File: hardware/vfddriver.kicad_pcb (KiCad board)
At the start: 2 copper layers, 75 x 40 mm, 36 parts, among them J1 Connection Header, U1 IVL2-5_7, U2 LM4871MX_NOPB, U3 LM2733YMF, U4 HV5812WG

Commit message: add research notes about vfds in general
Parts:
- R14: value 4.7kΩ -> 47kΩ

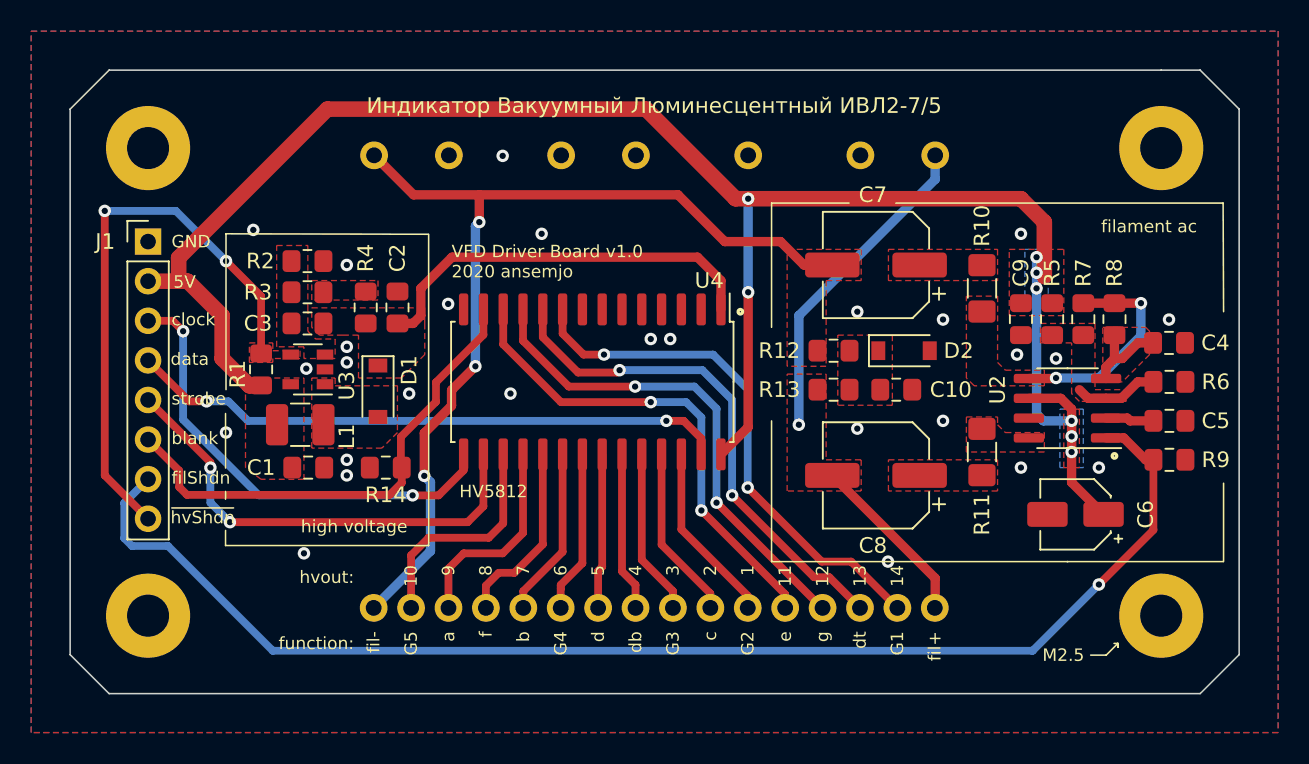
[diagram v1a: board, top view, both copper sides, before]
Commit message: hardware: tidy up, fix photodiode, (re)export (i)boms and schematics
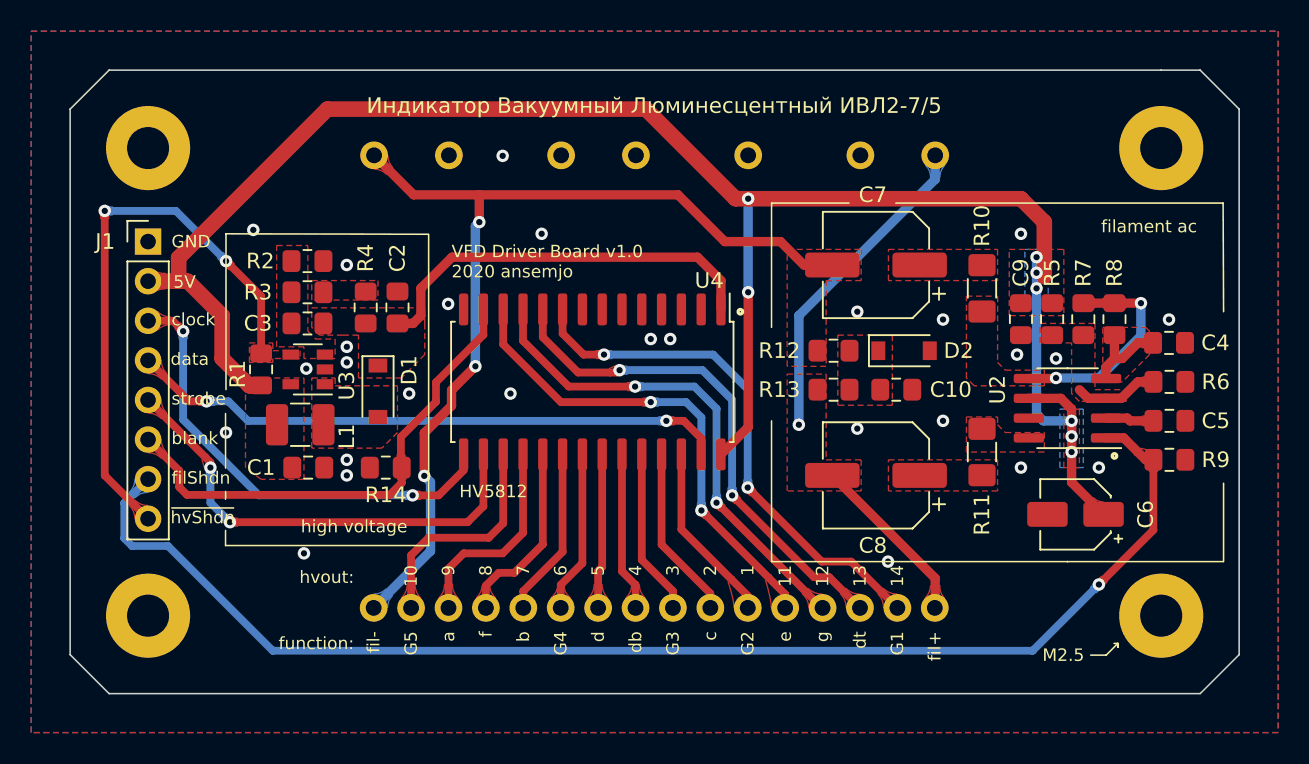
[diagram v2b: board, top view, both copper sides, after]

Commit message: hw: [WIP] add attiny412, remove traces in prep for v2
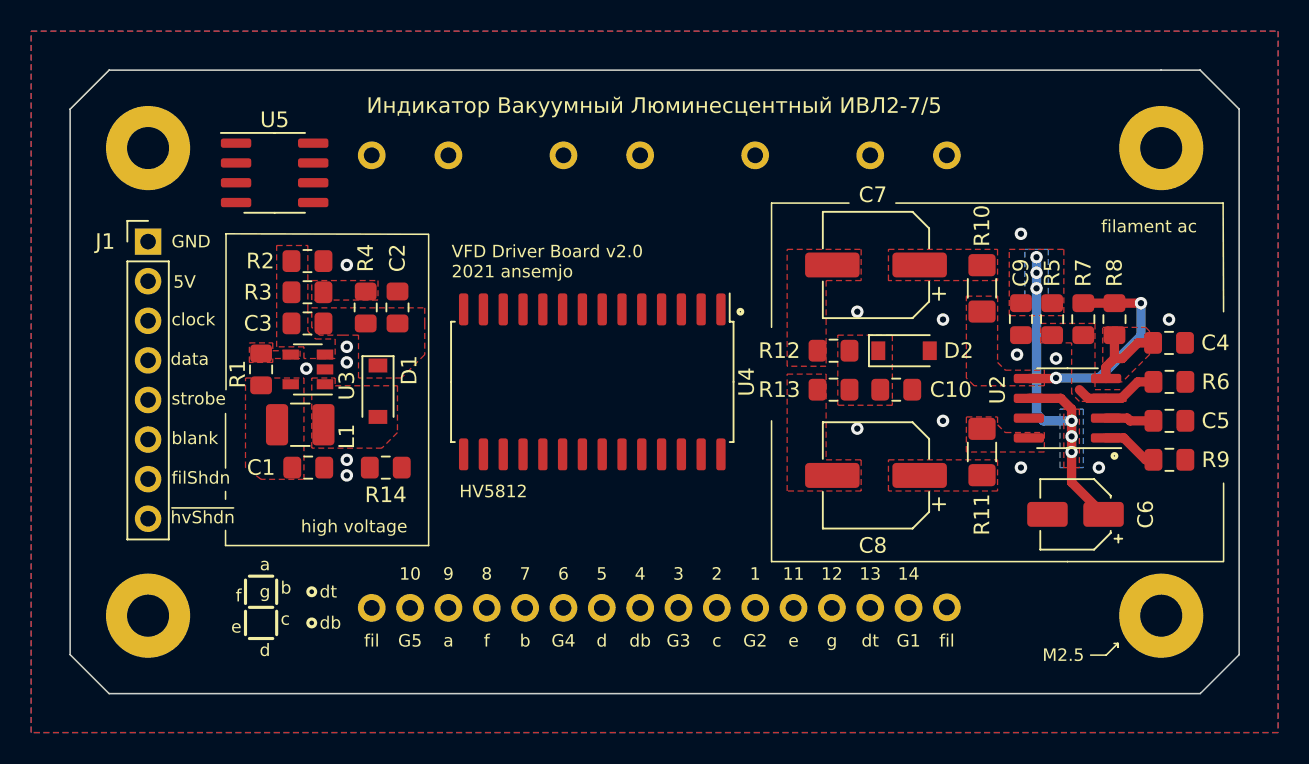
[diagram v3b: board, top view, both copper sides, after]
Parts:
- added U5: ATtiny412-SS, Package_SO:SOIC-8_3.9x4.9mm_P1.27mm, F.Cu at (98.1, 54.1)
- C1: value 2.2µF -> 4.7µF
- R10, R11: value 10Ω -> 12Ω 0.25W
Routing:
- net +5V: track 121.4 -> 25.1 mm, vias 8 -> 6
- net FIL_SHDN: track 84.8 -> 3.62 mm, vias 1 -> 0
- net FILAMENT-: track 62.0 -> 0.00 mm, vias 3 -> 0
- net HV_DATA: track 38.6 -> 0.00 mm, vias 2 -> 0
- net ~HV_SHDN~: track 36.9 -> 0.00 mm, vias 2 -> 0
- net /G1: track 34.0 -> 0.00 mm, vias 2 -> 0
- net /dt: track 33.0 -> 0.00 mm, vias 2 -> 0
- net FILAMENT+: track 32.2 -> 0.00 mm, vias 1 -> 0
- net HV_BLANK: track 32.0 -> 0.00 mm
- net /g: track 31.9 -> 0.00 mm, vias 2 -> 0
- net /e: track 31.3 -> 0.00 mm, vias 2 -> 0
- net HV_STROBE: track 30.0 -> 0.00 mm, vias 2 -> 0
- net HV_CLOCK: track 29.9 -> 0.00 mm, vias 2 -> 0
- net +24V: track 26.0 -> 0.00 mm
- net /G5: track 14.6 -> 0.00 mm
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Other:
- board text added: "VFD Driver Board v2.0 2021 ansemjo"
- board text added: "fil"
- board text removed: "VFD Driver Board v1.0 2020 ansemjo"
- board text removed: "fil+"
- board text removed: "fil-"
- board text removed: "function:"
- board text removed: "hvout:"
